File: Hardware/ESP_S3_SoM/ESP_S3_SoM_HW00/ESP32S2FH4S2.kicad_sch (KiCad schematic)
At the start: 31 parts, among them U401 ESP32-S2FH4, Y601 Crystal_GND24_Small

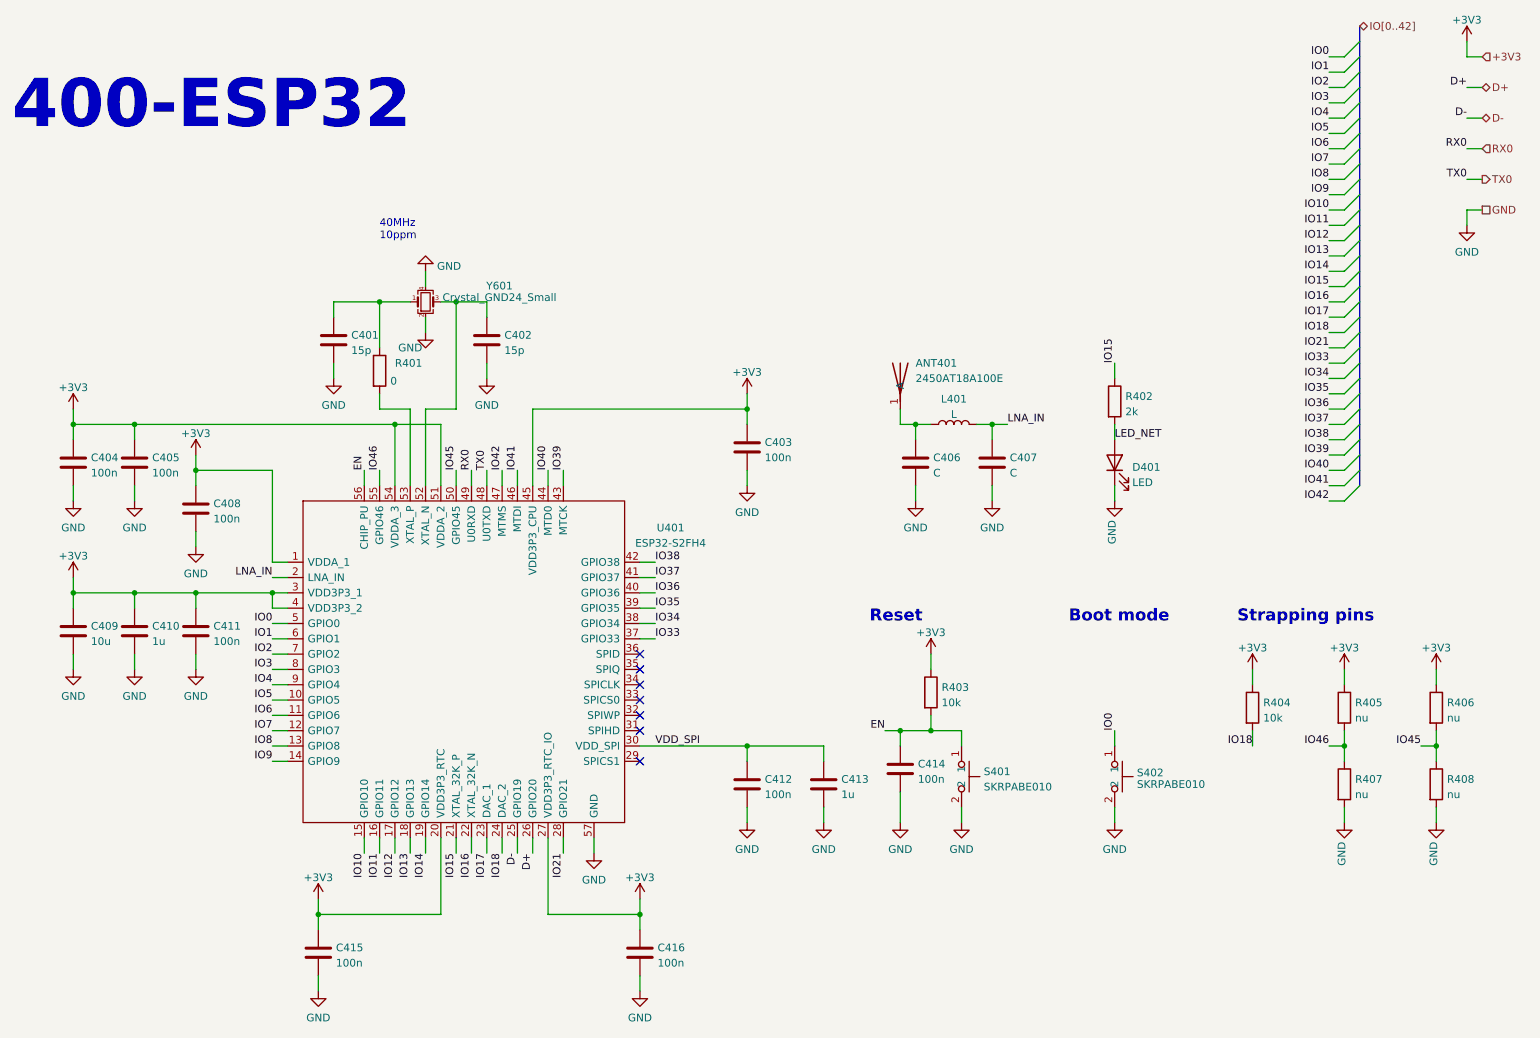
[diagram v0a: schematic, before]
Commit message: added SPI Bus
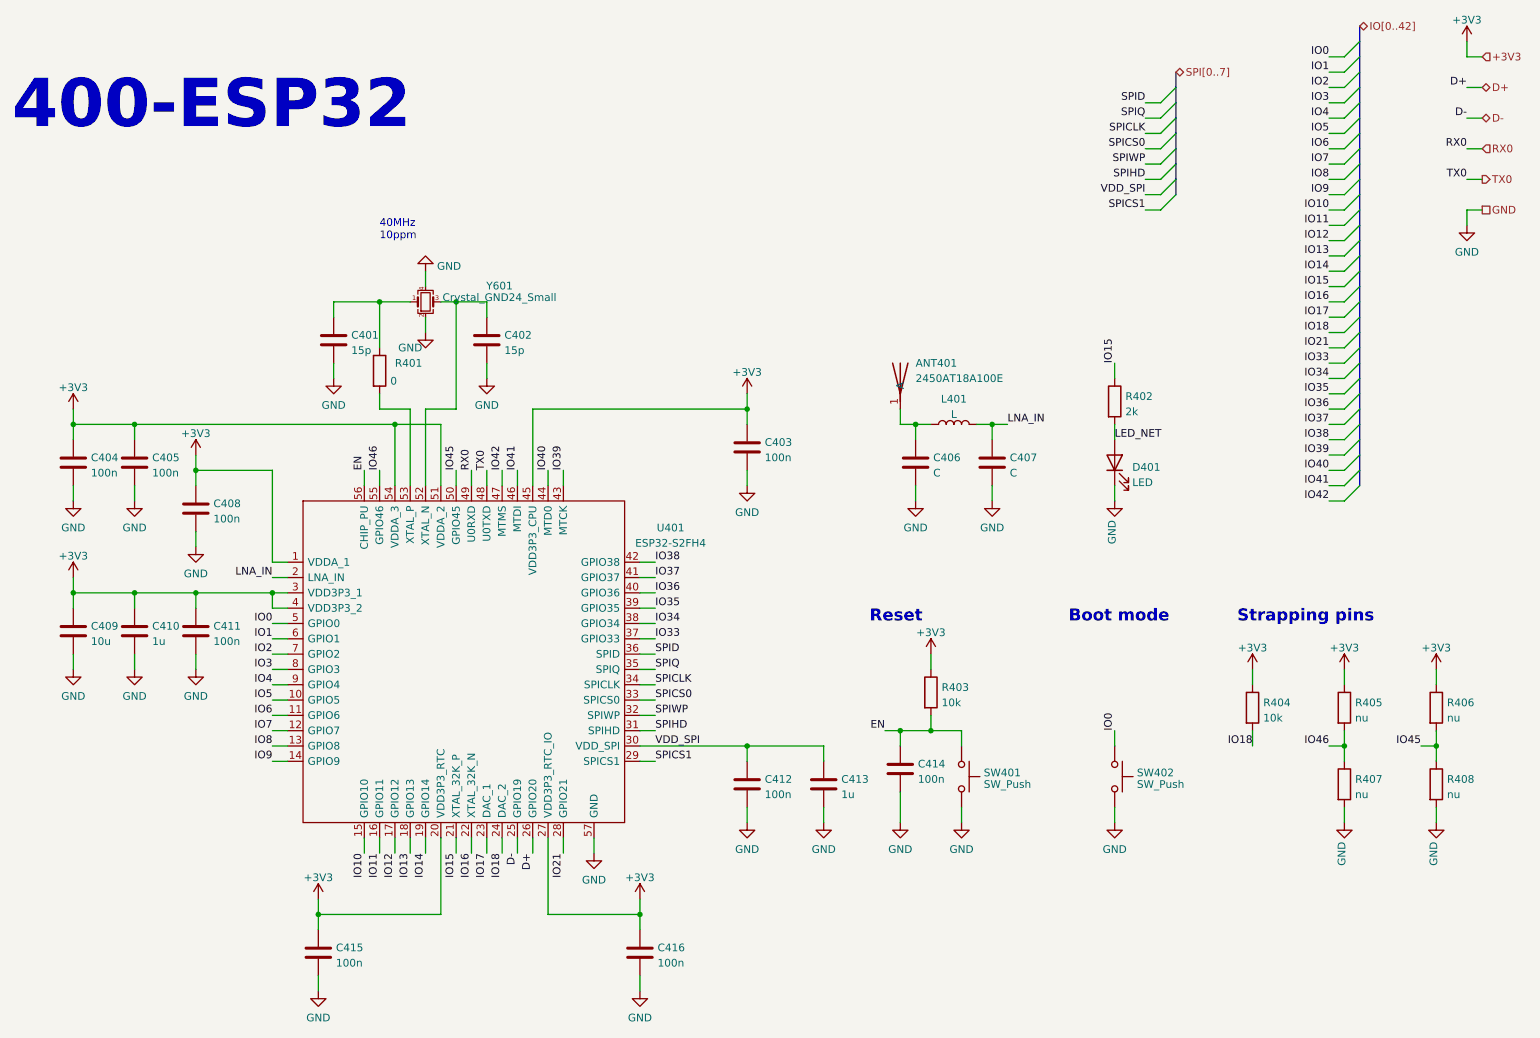
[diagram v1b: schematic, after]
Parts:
- removed S401, S402: SKRPABE010, Component_lib:SKRPABE010, symbol Component lib:SKRPABE010
- added SW401, SW402: SW_Push, Component_lib:B3U-1000P, symbol Switch:SW_Push
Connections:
- net EN: now also SW401.1
- net GND: now also SW401.2, SW402.2
- net IO0: now also SW402.1
- net SPICS1: now reaches U401.29 (SPICS1)
- net SPIHD: now reaches U401.31 (SPIHD)
- net SPIWP: now reaches U401.32 (SPIWP)
- net SPICS0: now reaches U401.33 (SPICS0)
- net SPICLK: now reaches U401.34 (SPICLK)
- net SPIQ: now reaches U401.35 (SPIQ)
- net SPID: now reaches U401.36 (SPID)
- no-connect marks 7 -> 0
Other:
- title: PMK_Keyboard -> PSoM - ESP S3
